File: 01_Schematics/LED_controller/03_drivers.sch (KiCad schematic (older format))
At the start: 76 parts, among them J14 PLD-14, J15 PLD-14, J16 Pin, J17 Pin, J18 Pin, J19 Pin, J20 TB-02, J21 TB-02, J22 Pin, J23 Pin, J24 Pin, J25 Pin, J26 Pin, J27 Pin, J28 PLD-14, J29 PLD-14, J30 Pin, J31 Pin, J32 Pin, J33 Pin, J34 TB-02, J35 TB-02, J36 Pin, J37 Pin, J38 Pin, J39 Pin, J40 Pin, J41 Pin, U3 MBI6651GSD, U4 MBI6651GSD, U5 MBI6651GSD, U6 MBI6651GSD

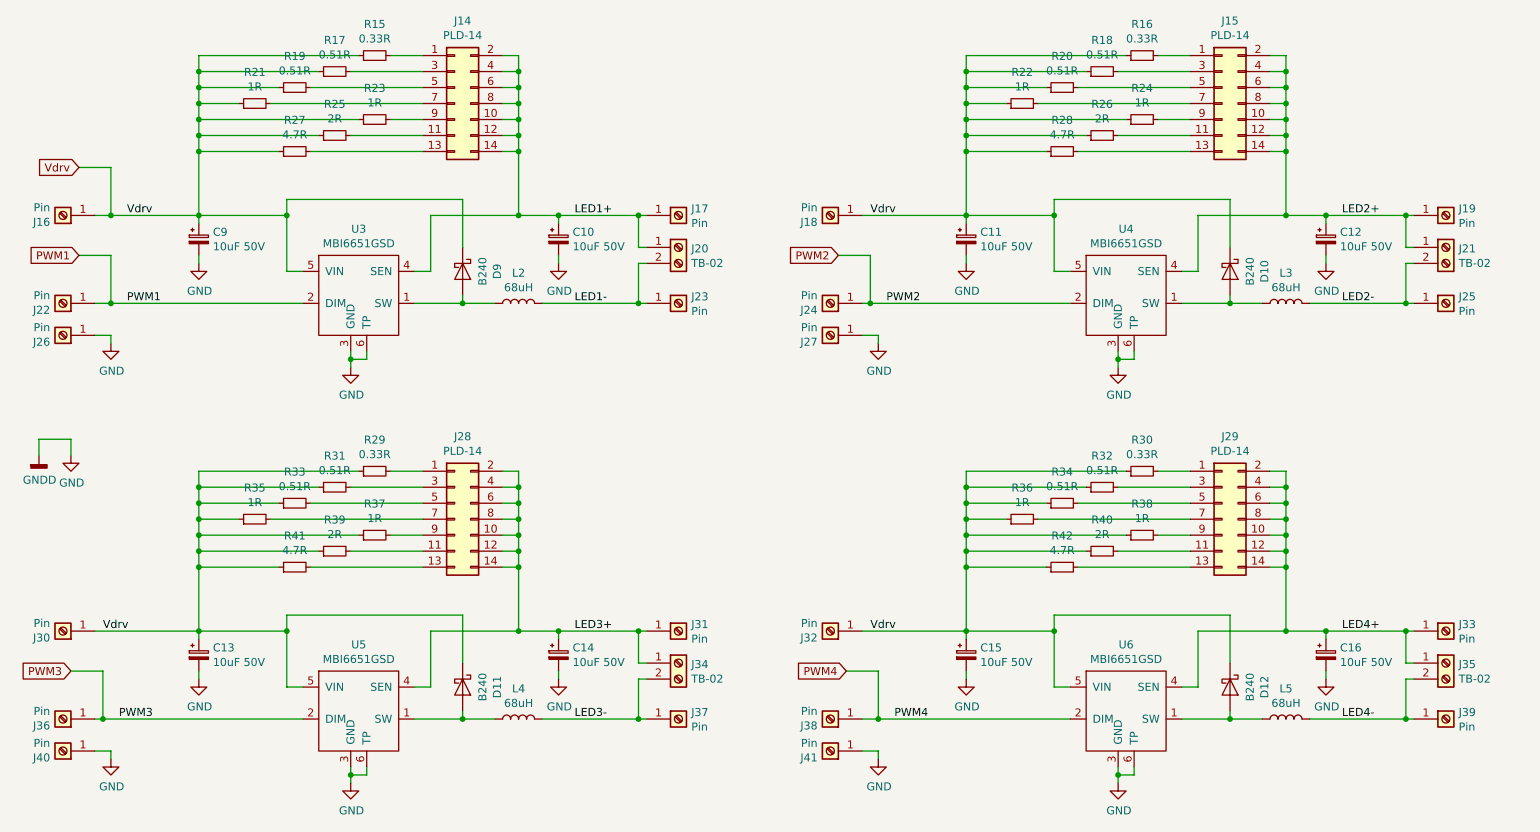
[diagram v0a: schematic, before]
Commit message: - Добавлена печатная плата; - Добавлены файлы посадочных мест использованных компонентов и STEP модели; - Добавлены файлы механической сборки (Solidworks);
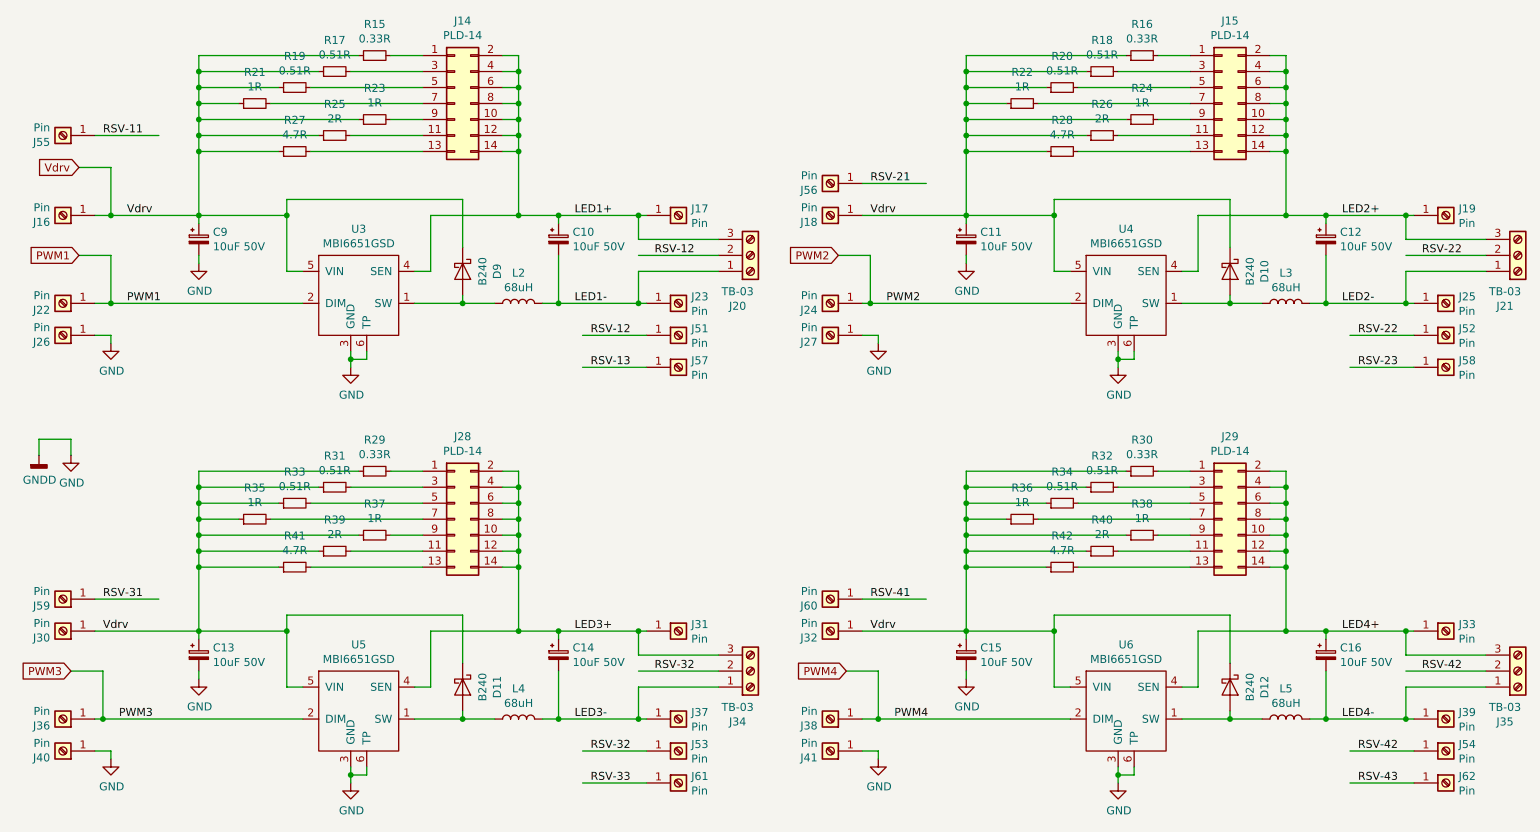
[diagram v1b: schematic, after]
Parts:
- removed J20, J21, J34, J35: TB-02, TerminalBlock:TerminalBlock_bornier-2_P5.08mm, symbol Connector:Screw_Terminal_01x02
- added J20, J21, J34, J35: TB-03, extras:TB-03_metric, symbol Connector:Screw_Terminal_01x03
- added J51, J52, J53, J54, J55, J56, J57, J58, J59, J60, J61, J62: Pin, TestPoint:TestPoint_THTPad_2.0x2.0mm_Drill1.0mm, symbol Connector:Screw_Terminal_01x01
- L2, L3, L4, L5: footprint Inductor_SMD:L_Bourns-SRR1005 -> extras:L_Bourns-SRR1005
- U3, U4, U5, U6: footprint Package_TO_SOT_SMD:TO-252-5_TabPin6 -> extras:TO-252-5L
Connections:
- net labels added: RSV-11, RSV-12, RSV-13, RSV-21, RSV-22, RSV-23, RSV-31, RSV-32, RSV-33, RSV-41, RSV-42, RSV-43
- wire segments 290 -> 310
